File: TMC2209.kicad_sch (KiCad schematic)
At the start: 26 parts, among them J3 Conn_01x04_Male, U7 TMC2209-LA

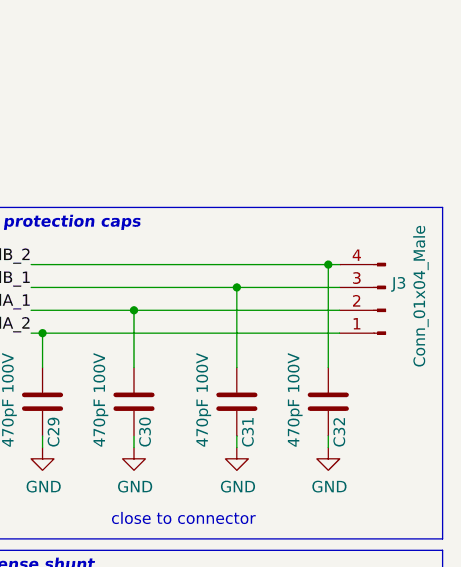
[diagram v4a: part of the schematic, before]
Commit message: Finish schematic
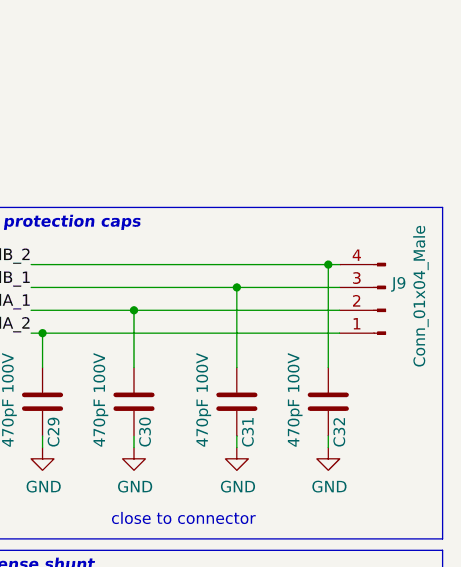
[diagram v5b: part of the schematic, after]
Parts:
- renumbered J3 to J9
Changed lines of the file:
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@@
   (symbol (lib_id "Connector:Conn_01x04_Male") (at 276.86 86.36 180) (unit 1)
     (in_bom yes) (on_board yes)
-    (property "Reference" "J3" (id 0) (at 277.5712 83.3628 0)
+    (property "Reference" "J9" (id 0) (at 277.5712 83.3628 0)
       (effects (font (size 1.27 1.27)) (justify right))
     )
@@
   (symbol (lib_id "power:GND") (at 172.72 88.9 0) (unit 1)
     (in_bom yes) (on_board yes)
-    (property "Reference" "#PWR055" (id 0) (at 172.72 95.25 0)
+    (property "Reference" "#PWR066" (id 0) (at 172.72 95.25 0)
       (effects (font (size 1.27 1.27)) hide)
     )
@@
   (symbol (lib_id "power:GND") (at 71.12 142.24 0) (unit 1)
     (in_bom yes) (on_board yes)
-    (property "Reference" "#PWR067" (id 0) (at 71.12 148.59 0)
+    (property "Reference" "#PWR078" (id 0) (at 71.12 148.59 0)
       (effects (font (size 1.27 1.27)) hide)
     )
@@
   (symbol (lib_id "power:GND") (at 104.14 53.34 0) (unit 1)
     (in_bom yes) (on_board yes)
-    (property "Reference" "#PWR050" (id 0) (at 104.14 59.69 0)
+    (property "Reference" "#PWR061" (id 0) (at 104.14 59.69 0)
       (effects (font (size 1.27 1.27)) hide)
     )
@@
   (symbol (lib_id "power:GND") (at 17.78 142.24 0) (unit 1)
     (in_bom yes) (on_board yes)
-    (property "Reference" "#PWR066" (id 0) (at 17.78 148.59 0)
+    (property "Reference" "#PWR077" (id 0) (at 17.78 148.59 0)
       (effects (font (size 1.27 1.27)) hide)
     )
@@
   (symbol (lib_id "power:GND") (at 107.95 40.64 0) (unit 1)
     (in_bom yes) (on_board yes)
-    (property "Reference" "#PWR047" (id 0) (at 107.95 46.99 0)
+    (property "Reference" "#PWR058" (id 0) (at 107.95 46.99 0)
       (effects (font (size 1.27 1.27)) hide)
     )
@@
   (symbol (lib_id "power:GND") (at 237.49 156.21 0) (unit 1)
     (in_bom yes) (on_board yes)
-    (property "Reference" "#PWR070" (id 0) (at 237.49 162.56 0)
+    (property "Reference" "#PWR081" (id 0) (at 237.49 162.56 0)
       (effects (font (size 1.27 1.27)) hide)
     )
@@
   (symbol (lib_id "power:GND") (at 260.35 156.21 0) (unit 1)
     (in_bom yes) (on_board yes)
-    (property "Reference" "#PWR071" (id 0) (at 260.35 162.56 0)
+    (property "Reference" "#PWR082" (id 0) (at 260.35 162.56 0)
       (effects (font (size 1.27 1.27)) hide)
     )
@@
   (symbol (lib_id "power:GND") (at 238.76 101.6 0) (unit 1)
     (in_bom yes) (on_board yes)
-    (property "Reference" "#PWR058" (id 0) (at 238.76 107.95 0)
+    (property "Reference" "#PWR069" (id 0) (at 238.76 107.95 0)
       (effects (font (size 1.27 1.27)) hide)
     )
@@
   (symbol (lib_id "power:GND") (at 248.92 101.6 0) (unit 1)
     (in_bom yes) (on_board yes)
-    (property "Reference" "#PWR059" (id 0) (at 248.92 107.95 0)
+    (property "Reference" "#PWR070" (id 0) (at 248.92 107.95 0)
       (effects (font (size 1.27 1.27)) hide)
     )
@@
   (symbol (lib_id "power:GND") (at 260.35 101.6 0) (unit 1)
     (in_bom yes) (on_board yes)
-    (property "Reference" "#PWR060" (id 0) (at 260.35 107.95 0)
+    (property "Reference" "#PWR071" (id 0) (at 260.35 107.95 0)
       (effects (font (size 1.27 1.27)) hide)
     )
@@
   (symbol (lib_id "power:GND") (at 270.51 101.6 0) (unit 1)
     (in_bom yes) (on_board yes)
-    (property "Reference" "#PWR061" (id 0) (at 270.51 107.95 0)
+    (property "Reference" "#PWR072" (id 0) (at 270.51 107.95 0)
       (effects (font (size 1.27 1.27)) hide)
     )
@@
   (symbol (lib_id "power:GND") (at 17.78 52.07 0) (unit 1)
     (in_bom yes) (on_board yes)
-    (property "Reference" "#PWR049" (id 0) (at 17.78 58.42 0)
+    (property "Reference" "#PWR060" (id 0) (at 17.78 58.42 0)
       (effects (font (size 1.27 1.27)) hide)
     )
@@
   (symbol (lib_id "power:VCC") (at 17.78 44.45 0) (unit 1)
     (in_bom yes) (on_board yes)
-    (property "Reference" "#PWR048" (id 0) (at 17.78 48.26 0)
+    (property "Reference" "#PWR059" (id 0) (at 17.78 48.26 0)
       (effects (font (size 1.27 1.27)) hide)
     )
@@
   (symbol (lib_id "power:VCC") (at 17.78 64.77 0) (unit 1)
     (in_bom yes) (on_board yes)
-    (property "Reference" "#PWR051" (id 0) (at 17.78 68.58 0)
+    (property "Reference" "#PWR062" (id 0) (at 17.78 68.58 0)
       (effects (font (size 1.27 1.27)) hide)
     )
@@
   (symbol (lib_id "power:VCC") (at 36.83 130.81 0) (unit 1)
     (in_bom yes) (on_board yes)
-    (property "Reference" "#PWR063" (id 0) (at 36.83 134.62 0)
+    (property "Reference" "#PWR074" (id 0) (at 36.83 134.62 0)
       (effects (font (size 1.27 1.27)) hide)
     )
@@
   (symbol (lib_id "power:VCC") (at 120.65 96.52 0) (unit 1)
     (in_bom yes) (on_board yes)
-    (property "Reference" "#PWR057" (id 0) (at 120.65 100.33 0)
+    (property "Reference" "#PWR068" (id 0) (at 120.65 100.33 0)
       (effects (font (size 1.27 1.27)) hide)
     )
@@
   (symbol (lib_id "power:+3V3") (at 125.73 86.36 0) (unit 1)
     (in_bom yes) (on_board yes)
-    (property "Reference" "#PWR054" (id 0) (at 125.73 90.17 0)
+    (property "Reference" "#PWR065" (id 0) (at 125.73 90.17 0)
       (effects (font (size 1.27 1.27)) hide)
     )
@@
   (symbol (lib_id "power:+3V3") (at 17.78 132.08 0) (unit 1)
     (in_bom yes) (on_board yes)
-    (property "Reference" "#PWR064" (id 0) (at 17.78 135.89 0)
+    (property "Reference" "#PWR075" (id 0) (at 17.78 135.89 0)
       (effects (font (size 1.27 1.27)) hide)
     )
@@
   (symbol (lib_id "power:GND") (at 17.78 72.39 0) (unit 1)
     (in_bom yes) (on_board yes)
-    (property "Reference" "#PWR053" (id 0) (at 17.78 78.74 0)
+    (property "Reference" "#PWR064" (id 0) (at 17.78 78.74 0)
       (effects (font (size 1.27 1.27)) hide)
     )
@@
   (symbol (lib_id "power:+3V3") (at 93.98 25.4 0) (unit 1)
     (in_bom yes) (on_board yes)
-    (property "Reference" "#PWR042" (id 0) (at 93.98 29.21 0)
+    (property "Reference" "#PWR053" (id 0) (at 93.98 29.21 0)
       (effects (font (size 1.27 1.27)) hide)
     )
@@
   (symbol (lib_id "power:GND") (at 43.18 26.67 90) (unit 1)
     (in_bom yes) (on_board yes)
-    (property "Reference" "#PWR044" (id 0) (at 49.53 26.67 0)
+    (property "Reference" "#PWR055" (id 0) (at 49.53 26.67 0)
       (effects (font (size 1.27 1.27)) hide)
     )
@@
   (symbol (lib_id "power:GND") (at 101.6 38.1 0) (unit 1)
     (in_bom yes) (on_board yes)
-    (property "Reference" "#PWR046" (id 0) (at 101.6 44.45 0)
+    (property "Reference" "#PWR057" (id 0) (at 101.6 44.45 0)
       (effects (font (size 1.27 1.27)) hide)
     )
@@
   (symbol (lib_id "power:GND") (at 102.87 27.94 0) (unit 1)
     (in_bom yes) (on_board yes)
-    (property "Reference" "#PWR045" (id 0) (at 102.87 34.29 0)
+    (property "Reference" "#PWR056" (id 0) (at 102.87 34.29 0)
       (effects (font (size 1.27 1.27)) hide)
     )
@@
   (symbol (lib_id "power:VCC") (at 22.86 26.67 90) (unit 1)
     (in_bom yes) (on_board yes)
-    (property "Reference" "#PWR043" (id 0) (at 26.67 26.67 0)
+    (property "Reference" "#PWR054" (id 0) (at 26.67 26.67 0)
       (effects (font (size 1.27 1.27)) hide)
     )
@@
   (symbol (lib_id "power:+3V3") (at 196.85 137.16 0) (unit 1)
     (in_bom yes) (on_board yes)
-    (property "Reference" "#PWR065" (id 0) (at 196.85 140.97 0)
+    (property "Reference" "#PWR076" (id 0) (at 196.85 140.97 0)
       (effects (font (size 1.27 1.27)) hide)
     )
@@
   (symbol (lib_id "power:GND") (at 196.85 157.48 0) (unit 1)
     (in_bom yes) (on_board yes)
-    (property "Reference" "#PWR072" (id 0) (at 196.85 163.83 0)
+    (property "Reference" "#PWR083" (id 0) (at 196.85 163.83 0)
       (effects (font (size 1.27 1.27)) hide)
     )
@@
   (symbol (lib_id "power:+3V3") (at 128.27 68.58 0) (unit 1)
     (in_bom yes) (on_board yes)
-    (property "Reference" "#PWR052" (id 0) (at 128.27 72.39 0)
+    (property "Reference" "#PWR063" (id 0) (at 128.27 72.39 0)
       (effects (font (size 1.27 1.27)) hide)
     )
@@
   (symbol (lib_id "power:VCC") (at 20.32 96.52 0) (unit 1)
     (in_bom yes) (on_board yes)
-    (property "Reference" "#PWR056" (id 0) (at 20.32 100.33 0)
+    (property "Reference" "#PWR067" (id 0) (at 20.32 100.33 0)
       (effects (font (size 1.27 1.27)) hide)
     )
@@
   (symbol (lib_id "power:GND") (at 20.32 106.68 0) (unit 1)
     (in_bom yes) (on_board yes)
-    (property "Reference" "#PWR062" (id 0) (at 20.32 113.03 0)
+    (property "Reference" "#PWR073" (id 0) (at 20.32 113.03 0)
       (effects (font (size 1.27 1.27)) hide)
     )
@@
   (symbol (lib_id "power:GND") (at 157.48 151.13 0) (unit 1)
     (in_bom yes) (on_board yes)
-    (property "Reference" "#PWR068" (id 0) (at 157.48 157.48 0)
+    (property "Reference" "#PWR079" (id 0) (at 157.48 157.48 0)
       (effects (font (size 1.27 1.27)) hide)
     )
@@
   (symbol (lib_id "power:GND") (at 170.18 151.13 0) (unit 1)
     (in_bom yes) (on_board yes)
-    (property "Reference" "#PWR069" (id 0) (at 170.18 157.48 0)
-      (effects (font (size 1.27 1.27)) hide)
-    )
+    (property "Reference" "#PWR080" (id 0) (at 170.18 157.48 0)
+      (effects (font (size 1.27 1.27)) hide)
+    )

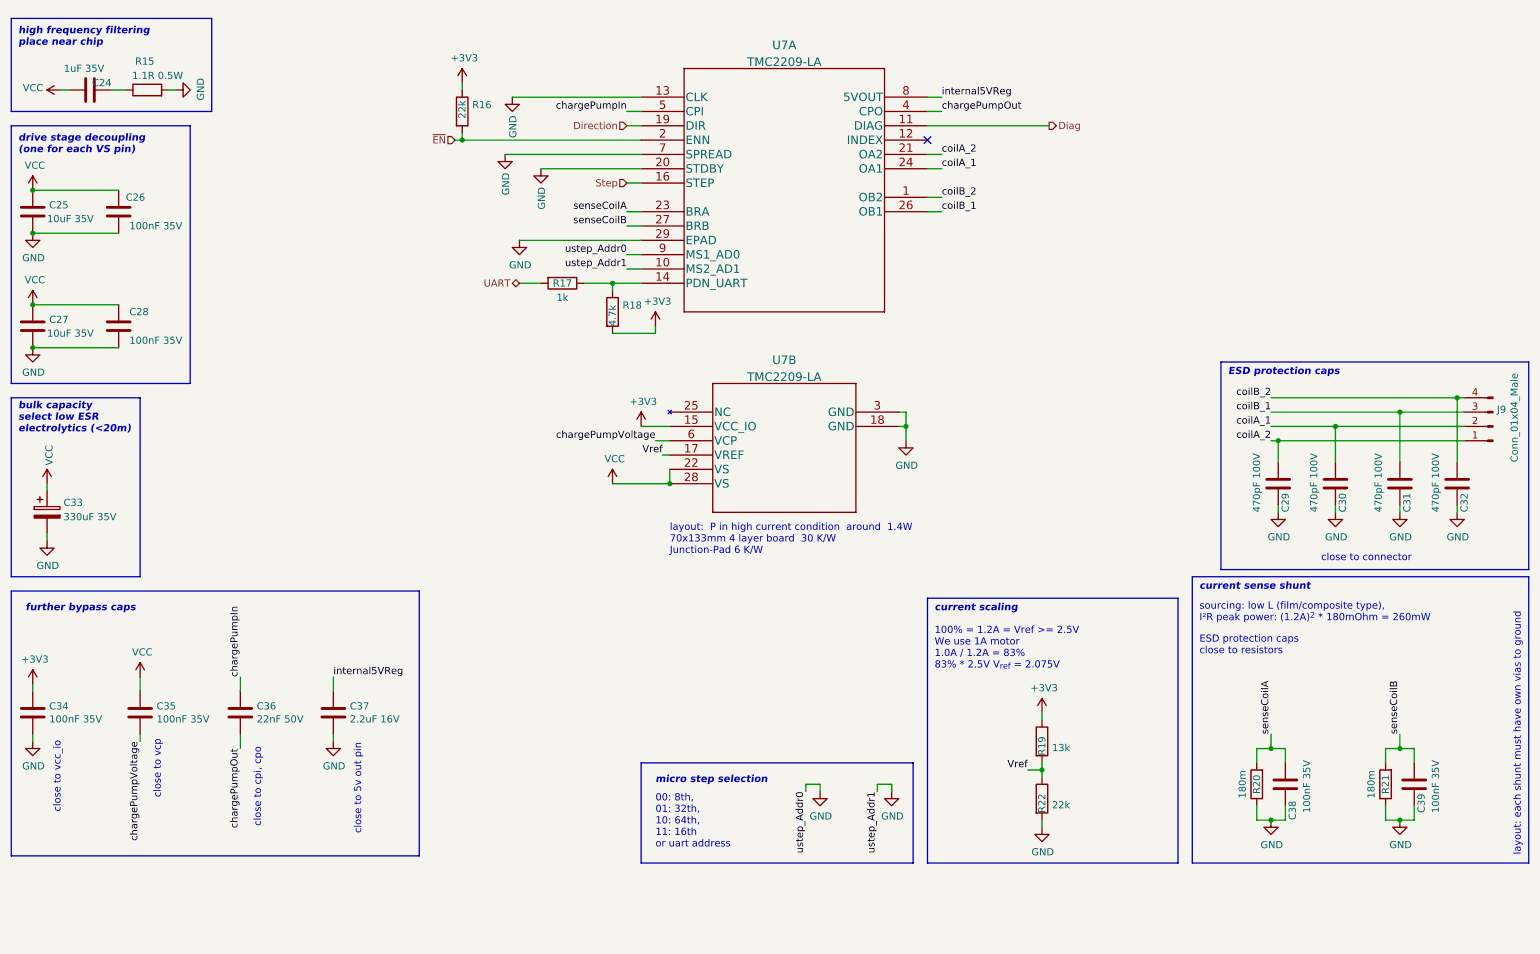
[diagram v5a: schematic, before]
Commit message: Add many changes to schematic and WIP PCB
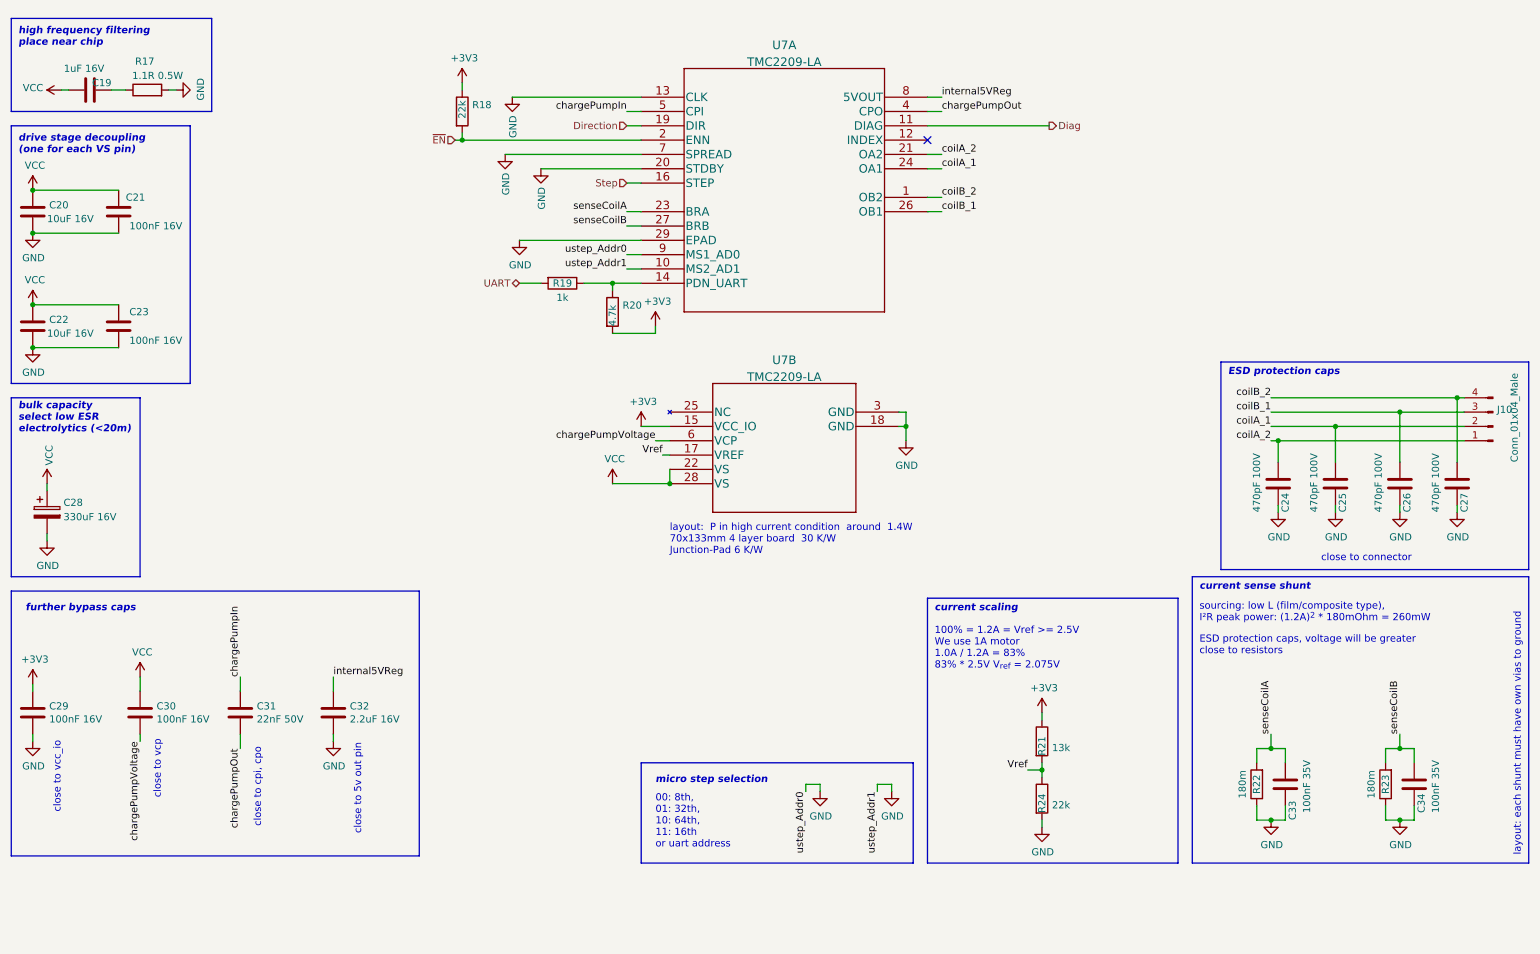
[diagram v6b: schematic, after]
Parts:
- C19: renamed from C24; value 1uF 35V -> 1uF 16V
- C20: renamed from C25; value 10uF 35V -> 10uF 16V
- C21: renamed from C26; value 100nF 35V -> 100nF 16V
- C22: renamed from C27; value 10uF 35V -> 10uF 16V
- C23: renamed from C28; value 100nF 35V -> 100nF 16V
- C28: renamed from C33; value 330uF 35V -> 330uF 16V
- C29: renamed from C34; value 100nF 35V -> 100nF 16V
- C30: renamed from C35; value 100nF 35V -> 100nF 16V
- renumbered C29 to C24, C30 to C25, C31 to C26, C32 to C27, C36 to C31, C37 to C32, C38 to C33, C39 to C34, J9 to J10, R15 to R17, R16 to R18, R17 to R19, R18 to R20, R19 to R21, R20 to R22, R21 to R23, R22 to R24
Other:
- note added: "ESD protection caps, voltage will be greater close to resistors"
- note removed: "ESD protection caps close to resistors"

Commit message: Some changes to schematic
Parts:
- J10: value Conn_01x04_Male -> Stepper
- R20: value 4.7k -> 4k7
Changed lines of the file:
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@@
       (effects (font (size 1.27 1.27)) (justify right))
     )
-    (property "Value" "Conn_01x04_Male" (id 1) (at 280.67 92.71 90)
-      (effects (font (size 1.27 1.27)) (justify right))
+    (property "Value" "Stepper" (id 1) (at 280.67 92.71 90)
+      (effects (font (size 1.27 1.27)) (justify right) hide)
     )
     (property "Footprint" "Connector_JST:JST_XH_B4B-XH-A_1x04_P2.50mm_Vertical" (id 2) (at 276.86 86.36 0)
@@
   (symbol (lib_id "Device:C") (at 27.94 26.67 90) (unit 1)
     (in_bom yes) (on_board yes)
-    (property "Reference" "C19" (id 0) (at 31.75 25.4 90)
-      (effects (font (size 1.27 1.27)) (justify left))
-    )
-    (property "Value" "1uF 16V" (id 1) (at 30.48 22.86 90)
+    (property "Reference" "C19" (id 0) (at 26.67 27.94 90)
+      (effects (font (size 1.27 1.27)) (justify left))
+    )
+    (property "Value" "1uF 16V" (id 1) (at 31.75 22.86 90)
       (effects (font (size 1.27 1.27)) (justify left))
     )
@@
   (symbol (lib_id "Device:R") (at 38.1 26.67 90) (unit 1)
     (in_bom yes) (on_board yes)
-    (property "Reference" "R17" (id 0) (at 39.37 21.59 90)
+    (property "Reference" "R17" (id 0) (at 40.005 26.67 90)
       (effects (font (size 1.27 1.27)) (justify left))
     )
@@
   (symbol (lib_id "Device:R") (at 93.98 30.48 0) (unit 1)
     (in_bom yes) (on_board yes)
-    (property "Reference" "R18" (id 0) (at 95.758 29.3116 0)
-      (effects (font (size 1.27 1.27)) (justify left))
-    )
-    (property "Value" "22k" (id 1) (at 93.98 31.75 90)
+    (property "Reference" "R18" (id 0) (at 93.98 32.385 90)
+      (effects (font (size 1.27 1.27)) (justify left))
+    )
+    (property "Value" "22k" (id 1) (at 95.25 31.115 0)
       (effects (font (size 1.27 1.27)) (justify left))
     )
@@
   (symbol (lib_id "Device:R") (at 120.65 66.04 0) (unit 1)
     (in_bom yes) (on_board yes)
-    (property "Reference" "R20" (id 0) (at 122.428 64.8716 0)
-      (effects (font (size 1.27 1.27)) (justify left))
-    )
-    (property "Value" "4.7k" (id 1) (at 120.65 68.58 90)
-      (effects (font (size 1.27 1.27)) (justify left))
-    )
+    (property "Reference" "R20" (id 0) (at 120.65 67.945 90)
+      (effects (font (size 1.27 1.27)) (justify left))
+    )
+    (property "Value" "4k7" (id 1) (at 122.555 67.945 0)
+      (effects (font (size 1.27 1.27)) (justify left))
+    )
